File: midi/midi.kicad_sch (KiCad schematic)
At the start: 21 parts, among them U1 ESP32-S3-WROOM-1-n16

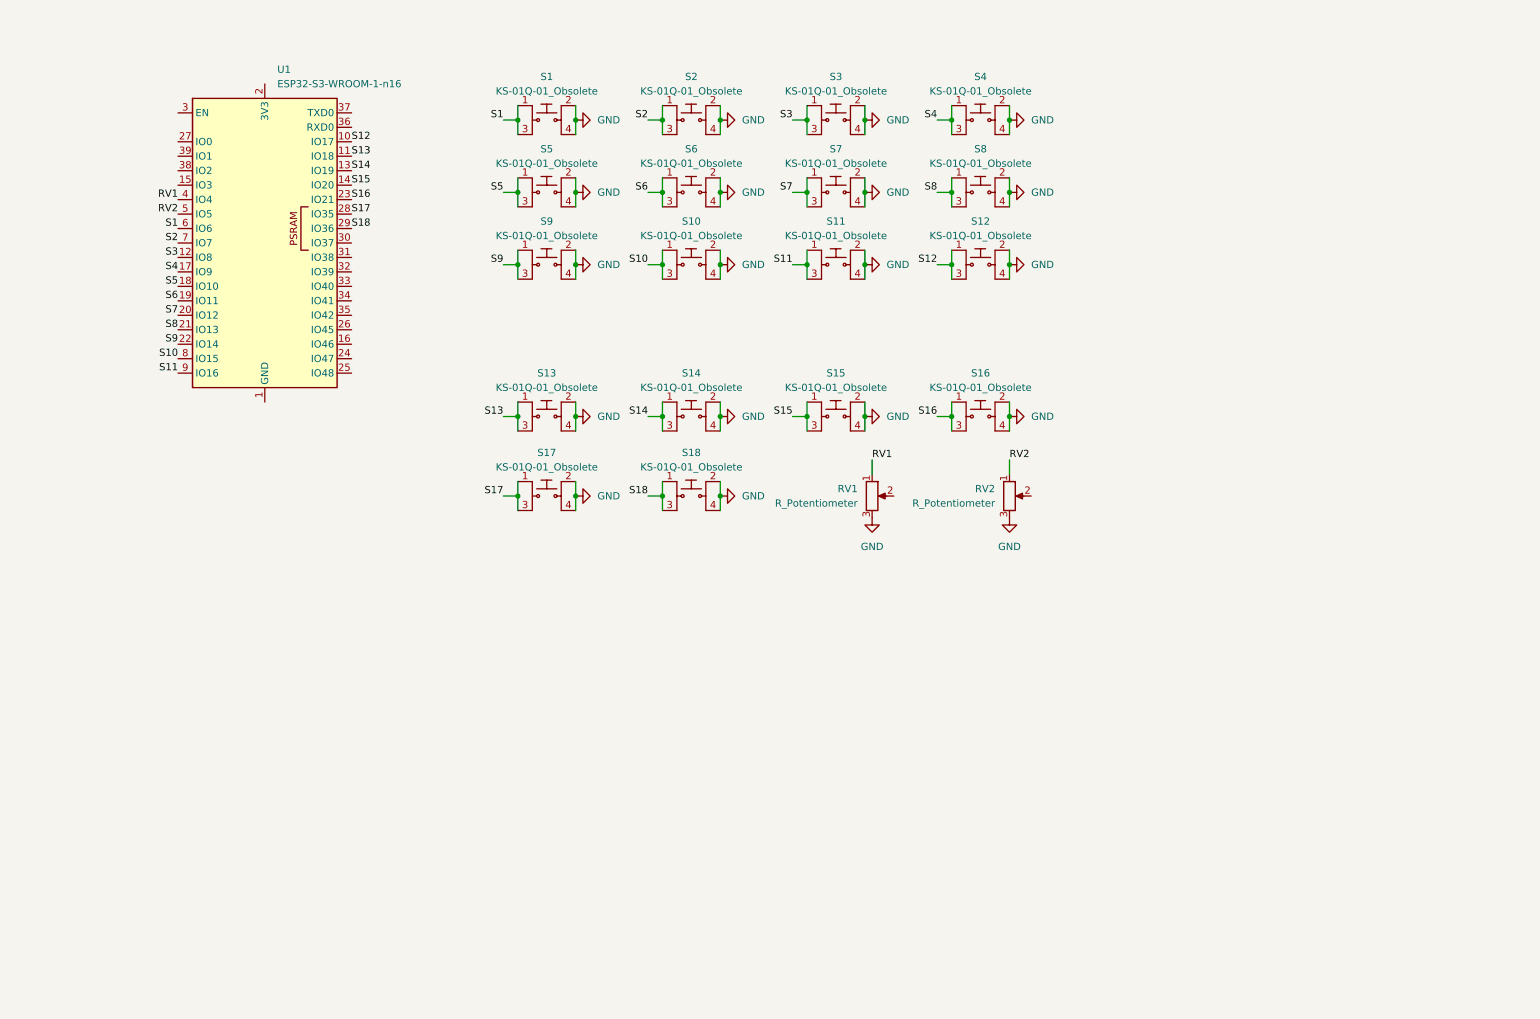
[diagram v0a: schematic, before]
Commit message: added LTC1624 symbol, button layout, working on voltage reg
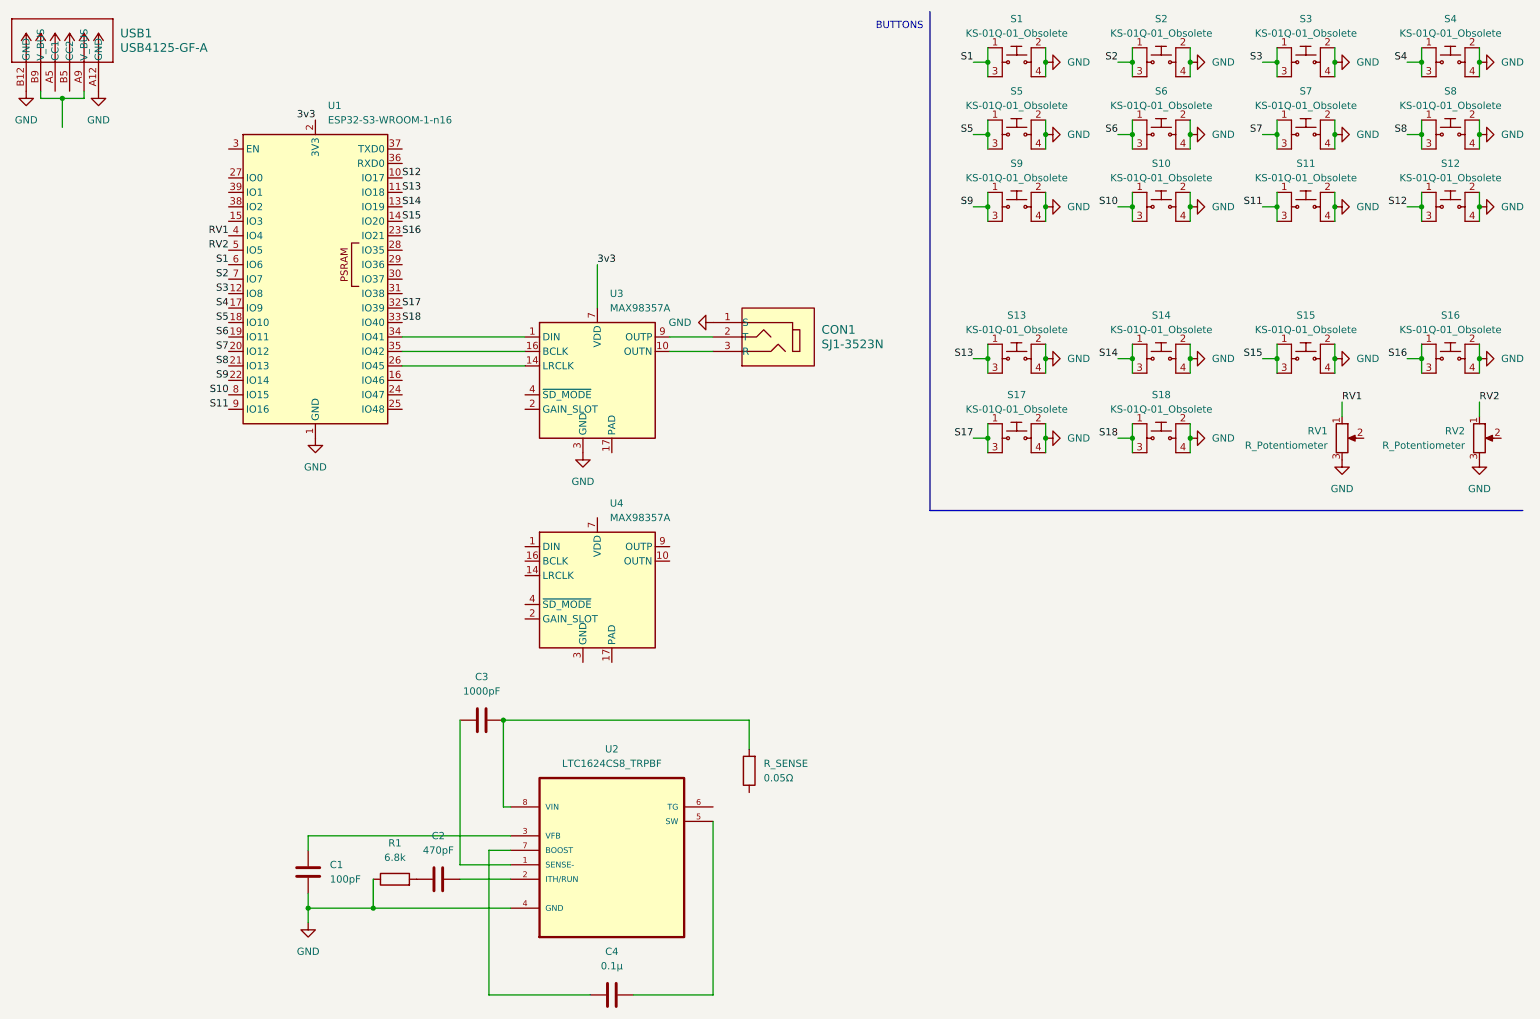
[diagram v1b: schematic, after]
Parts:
- added C1: 100pF, symbol Device:C
- added C2: 470pF, symbol Device:C
- added C3: 1000pF, symbol Device:C
- added C4: 0.1µ, symbol Device:C
- added CON1: SJ1-3523N, digikey-footprints:Headphone_Jack_3.5mm_SJ1-3523N, symbol dk_Barrel-Audio-Connectors:SJ1-3523N
- added R1: 6.8k, symbol Device:R
- added R_SENSE: 0.05Ω, symbol Device:R
- added U2: LTC1624CS8_TRPBF, LTC1624CS8_TRPBF:SOIC127P600X175-8N, symbol LTC1624CS8_TRPBF:LTC1624CS8_TRPBF
- added U3, U4: MAX98357A, Package_DFN_QFN:TQFN-16-1EP_3x3mm_P0.5mm_EP1.23x1.23mm, symbol Audio:MAX98357A
- added USB1: USB4125-GF-A, CONN6_USB4125_GCT, symbol USB4125_GF_A:USB4125-GF-A
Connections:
- net GND: now also U1.1 (GND), U1.40 (GND), U1.41 (GND), C1.2, CON1.1 (S), R1.1, U2.4 (GND), U3.11 (GND), U3.15 (GND), U3.3 (GND), USB1.A12 (GND), USB1.B12 (GND)
- net S17: now also U1.32 (IO39); no longer U1.28 (IO35)
- net S18: now also U1.33 (IO40); no longer U1.29 (IO36)
- net 3v3: now reaches U1.2 (3V3)
- net 3v3: now also U3.7 (VDD), U3.8 (VDD)
- net at U1.26 (IO45): now also U3.14 (LRCLK)
- net at U1.34 (IO41): now also U3.1 (DIN)
- net at U1.35 (IO42): now also U3.16 (BCLK)
- new net: C3.2, R_SENSE.2, U2.8 (VIN)
- new net: C2.1, R1.2
- new net: C2.2, U2.2 (ITH/RUN)
- new net: CON1.3 (R), U3.10 (OUTN)
- new net: CON1.2 (T), U3.9 (OUTP)
- new net: C3.1, U2.1 (SENSE-)
- new net: C1.1, U2.3 (VFB)
- new net: C4.1, U2.5 (SW)
- new net: C4.2, U2.7 (BOOST)
- new net: USB1.A9 (V_BUS), USB1.B9 (V_BUS)
- new net: U4.11 (GND), U4.15 (GND), U4.3 (GND)
- new net: U4.7 (VDD), U4.8 (VDD)
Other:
- note added: "BUTTONS"
- moved on the sheet: RV1, RV2, S1, S10, S11, S12, S13, S14, S15, S16, S17, S18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

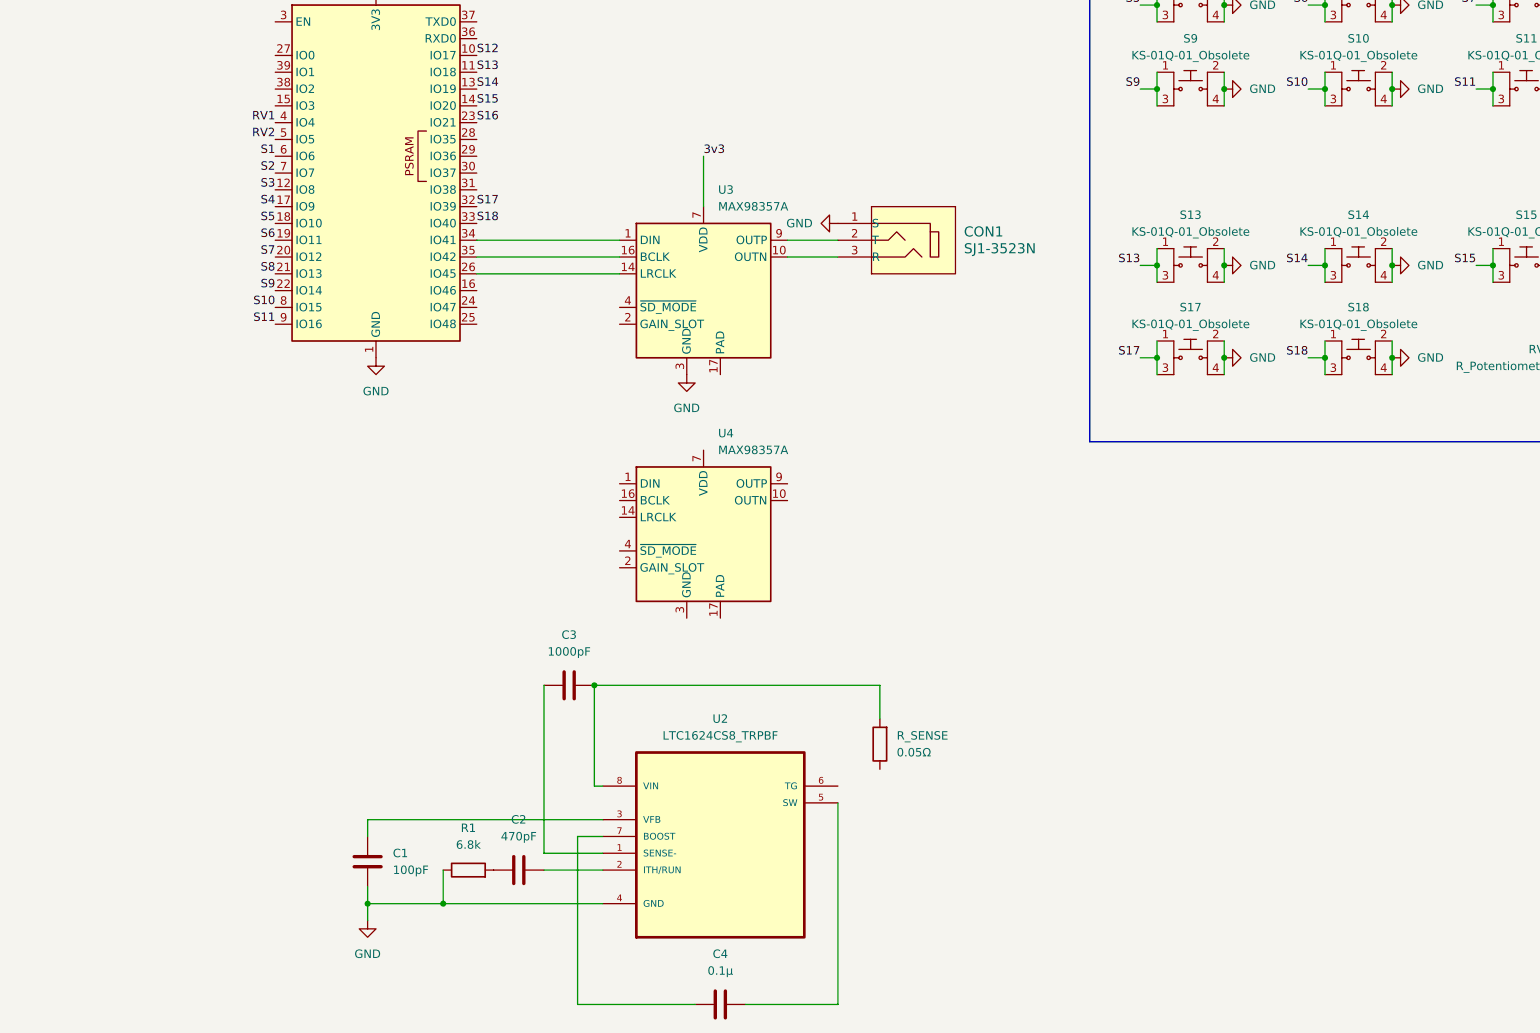
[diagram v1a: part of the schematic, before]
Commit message: finished voltage regulator
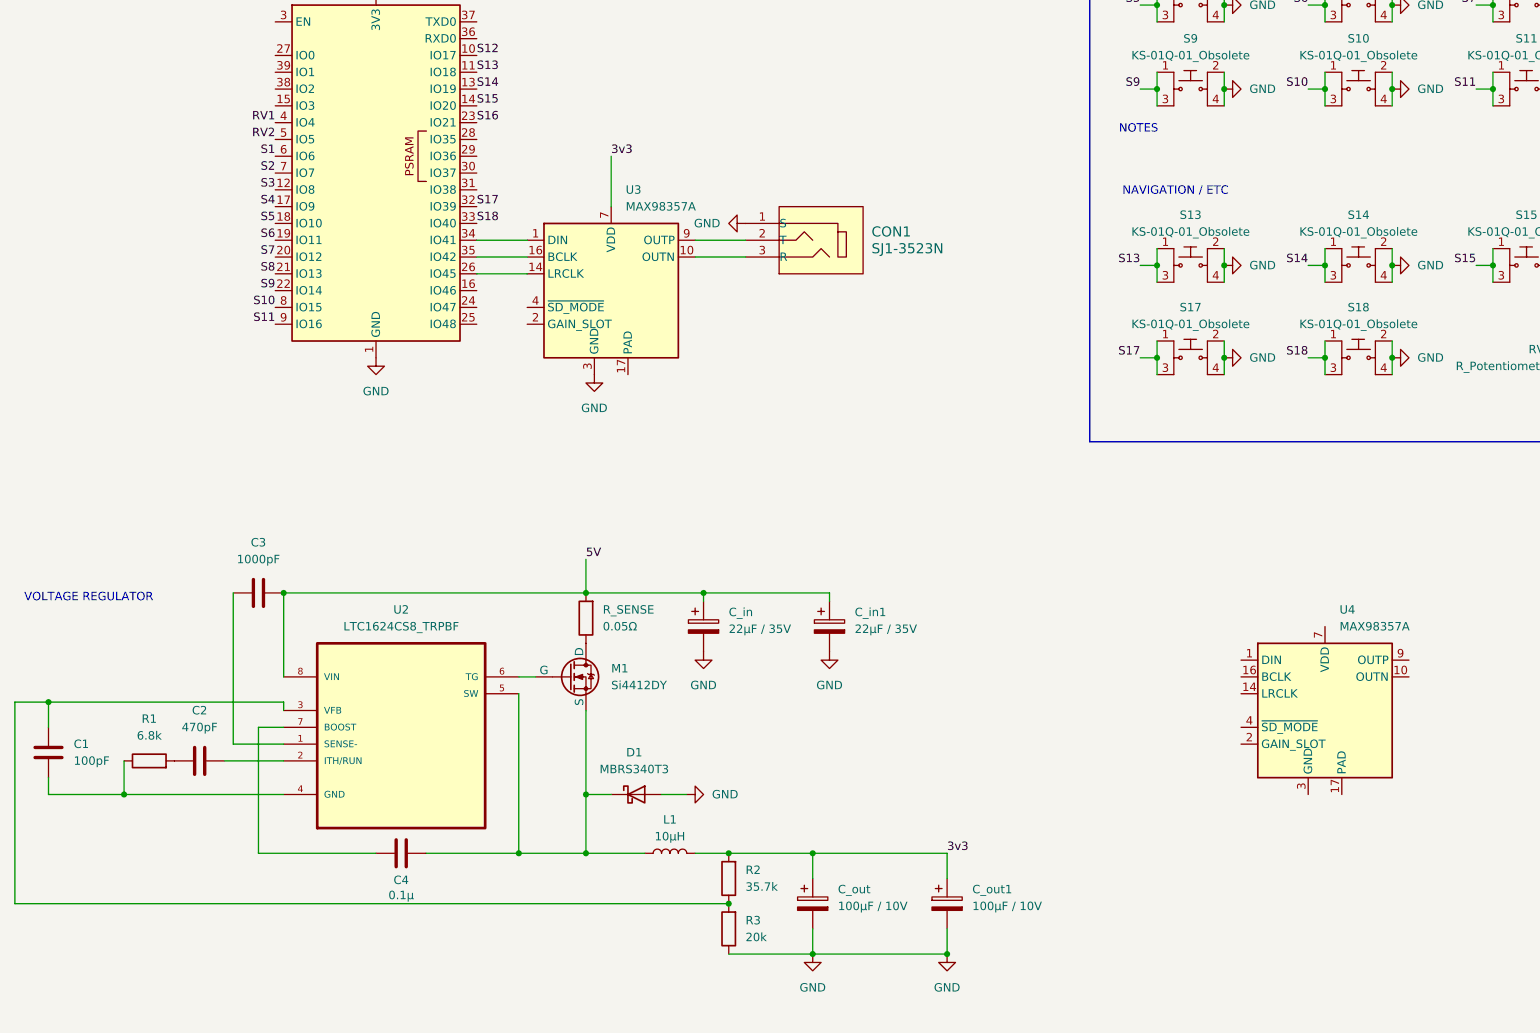
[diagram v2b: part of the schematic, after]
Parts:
- added C_in, C_in1: 22µF / 35V, symbol Device:C_Polarized
- added C_out, C_out1: 100µF / 10V, symbol Device:C_Polarized
- added D1: MBRS340T3, symbol Device:D_Schottky
- added L1: 10µH, symbol Device:L
- added M1: Si4412DY, symbol Simulation_SPICE:NMOS
- added R2: 35.7k, symbol Device:R
- added R3: 20k, symbol Device:R
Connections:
- net 3v3: now also C_out.1, C_out1.1, L1.2, R2.2
- net GND: now also C_in.2, C_in1.2, C_out.2, C_out1.2, D1.2 (A), R3.1; no longer C1.2, R1.1, U2.4 (GND)
- net at R_SENSE.1: now also M1.1 (D)
- net 5V: now reaches C3.2, R_SENSE.2, U2.8 (VIN)
- net 5V: now also C_in.1, C_in1.1
- net at C1.1, U2.3 (VFB): now also R2.1, R3.2
- net at U2.5 (SW): now also C4.2, D1.1 (K), L1.1, M1.3 (S); no longer C4.1
- net at U2.6 (TG): now also M1.2 (G)
- net at U2.7 (BOOST): now also C4.1; no longer C4.2
- new net: C1.2, R1.1, U2.4 (GND)
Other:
- note added: "NAVIGATION / ETC"
- note added: "NOTES"
- note added: "VOLTAGE REGULATOR"
- moved on the sheet: C1, C2, C3, C4, CON1, R1, R_SENSE, U2, U3, U4

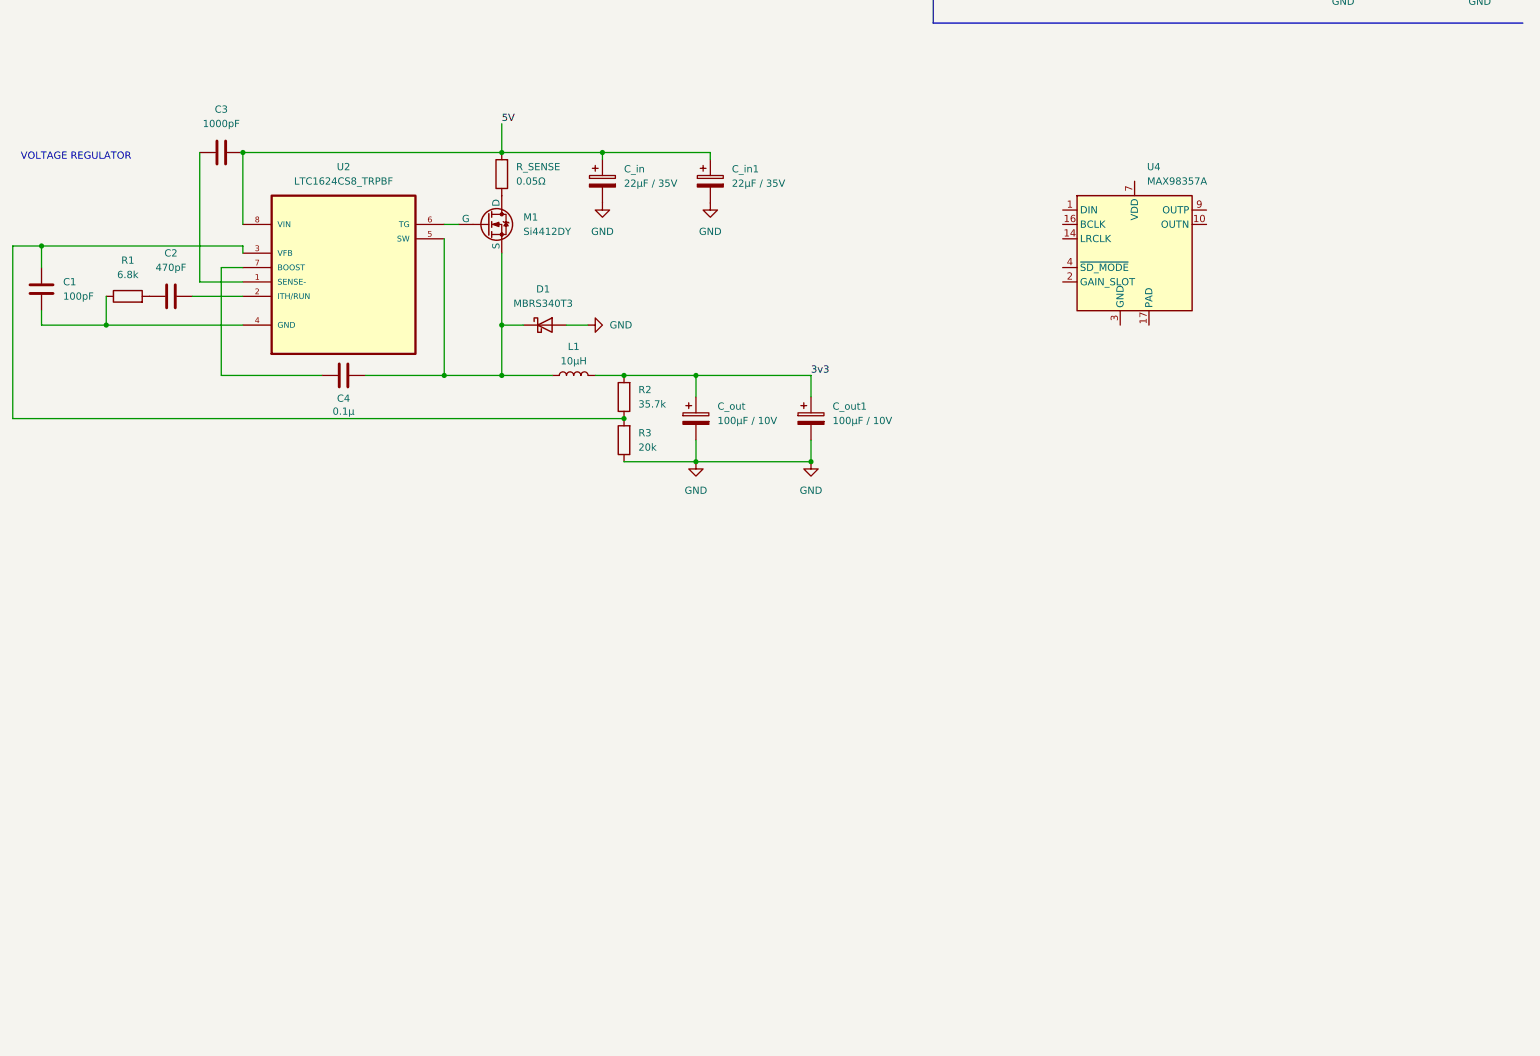
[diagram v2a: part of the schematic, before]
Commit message: page size increase and loaded screen
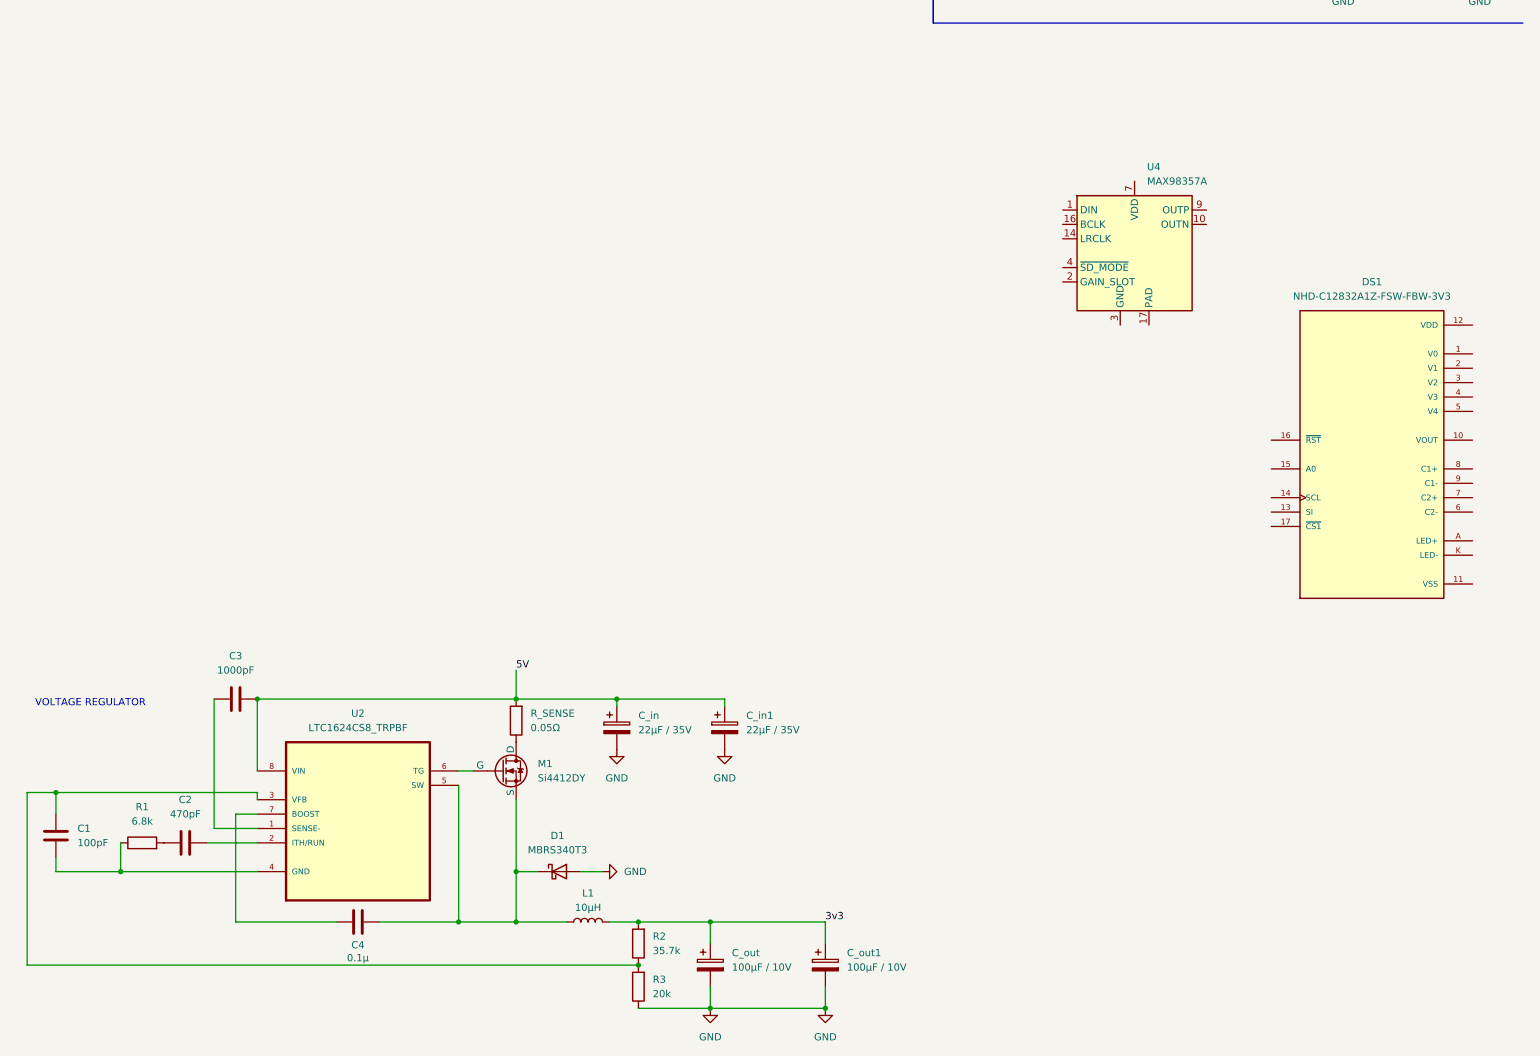
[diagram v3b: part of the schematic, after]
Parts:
- added DS1: NHD-C12832A1Z-FSW-FBW-3V3, NHD-C12832A1Z-FSW-FBW-3V3:LCD_NHD-C12832A1Z-FSW-FBW-3V3, symbol NHD-C12832A1Z-FSW-FBW-3V3:NHD-C12832A1Z-FSW-FBW-3V3
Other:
- moved on the sheet: C1, C2, C3, C4, C_in, C_in1, C_out, C_out1, D1, L1, M1, R1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
